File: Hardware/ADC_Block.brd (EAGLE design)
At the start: 30.5 x 44.5 mm, 33 parts, among them U1 ADS1015, U2 PCA9306, U3 3.3V

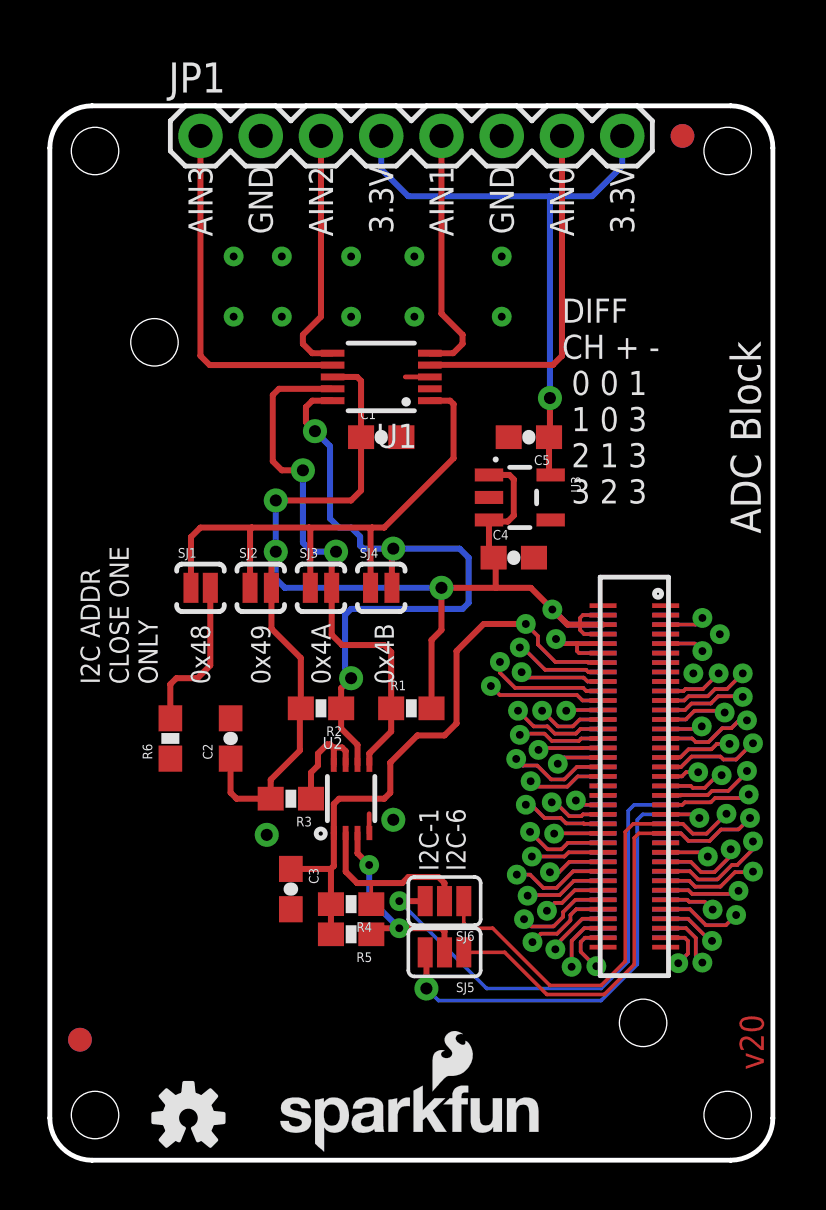
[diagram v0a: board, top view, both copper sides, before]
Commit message: moved differential pair chart and added separation lines
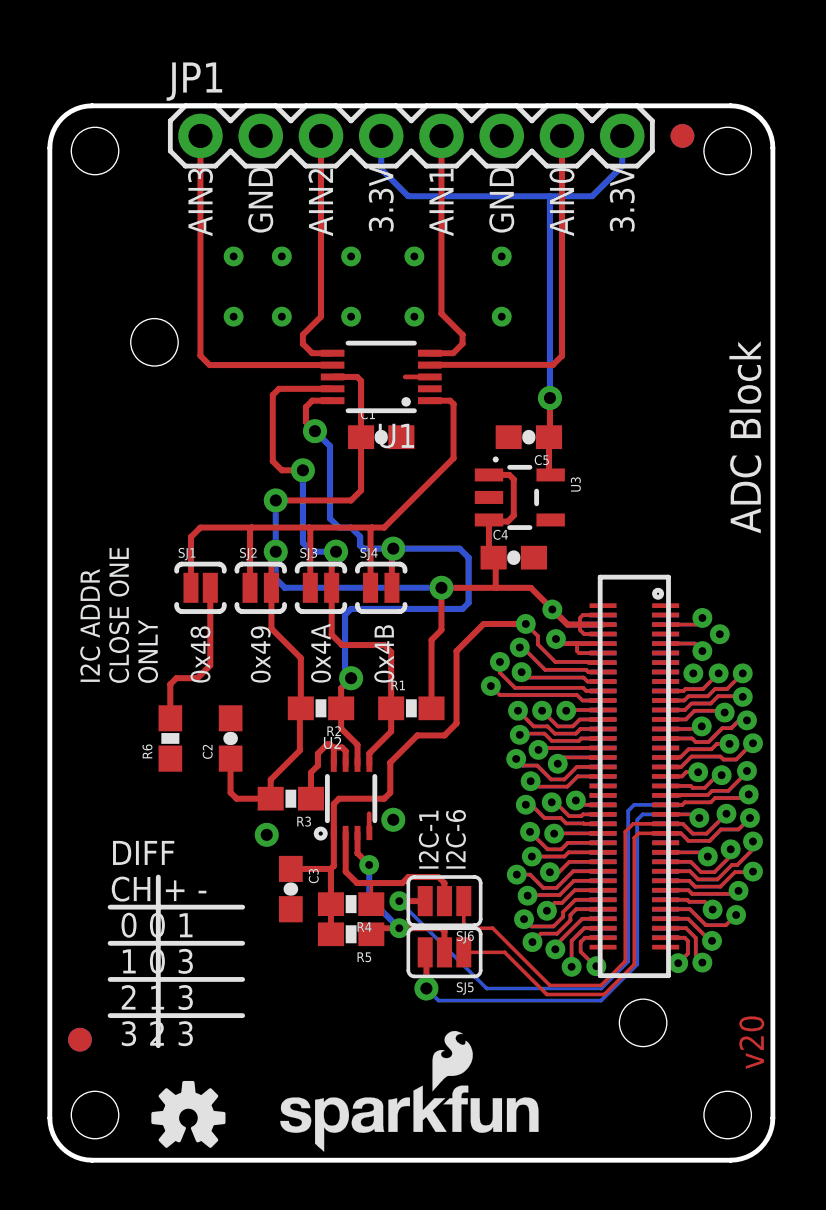
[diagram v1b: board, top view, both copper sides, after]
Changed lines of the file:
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@@
 <?xml version="1.0" encoding="utf-8"?>
 <!DOCTYPE eagle SYSTEM "eagle.dtd">
-<eagle version="7.3.0">
+<eagle version="7.1.0">
 <drawing>
 <settings>
@@
 <setting verticaltext="up"/>
 </settings>
-<grid distance="0.05" unitdist="inch" unit="inch" style="lines" multiple="1" display="yes" altdistance="0.005" altunitdist="inch" altunit="inch"/>
+<grid distance="0.01" unitdist="inch" unit="inch" style="lines" multiple="1" display="yes" altdistance="0.005" altunitdist="inch" altunit="inch"/>
 <layers>
 <layer number="1" name="Top" color="4" fill="1" visible="yes" active="yes"/>
-<layer number="2" name="Route2" color="1" fill="3" visible="no" active="yes"/>
-<layer number="15" name="Route15" color="4" fill="6" visible="no" active="yes"/>
+<layer number="2" name="Route2" color="1" fill="3" visible="yes" active="yes"/>
+<layer number="15" name="Route15" color="4" fill="6" visible="yes" active="yes"/>
 <layer number="16" name="Bottom" color="1" fill="1" visible="yes" active="yes"/>
 <layer number="17" name="Pads" color="2" fill="1" visible="yes" active="yes"/>
@@
 <layer number="23" name="tOrigins" color="15" fill="1" visible="yes" active="yes"/>
 <layer number="24" name="bOrigins" color="15" fill="1" visible="yes" active="yes"/>
-<layer number="25" name="tNames" color="7" fill="1" visible="no" active="yes"/>
-<layer number="26" name="bNames" color="7" fill="1" visible="no" active="yes"/>
-<layer number="27" name="tValues" color="7" fill="1" visible="no" active="yes"/>
-<layer number="28" name="bValues" color="7" fill="1" visible="no" active="yes"/>
-<layer number="29" name="tStop" color="7" fill="3" visible="no" active="yes"/>
-<layer number="30" name="bStop" color="7" fill="6" visible="no" active="yes"/>
-<layer number="31" name="tCream" color="7" fill="4" visible="no" active="yes"/>
-<layer number="32" name="bCream" color="7" fill="5" visible="no" active="yes"/>
-<layer number="39" name="tKeepout" color="4" fill="11" visible="no" active="yes"/>
-<layer number="40" name="bKeepout" color="1" fill="11" visible="no" active="yes"/>
-<layer number="41" name="tRestrict" color="4" fill="10" visible="no" active="yes"/>
-<layer number="42" name="bRestrict" color="1" fill="10" visible="no" active="yes"/>
-<layer number="43" name="vRestrict" color="2" fill="10" visible="no" active="yes"/>
-<layer number="44" name="Drills" color="7" fill="1" visible="no" active="yes"/>
+<layer number="25" name="tNames" color="7" fill="1" visible="yes" active="yes"/>
+<layer number="26" name="bNames" color="7" fill="1" visible="yes" active="yes"/>
+<layer number="27" name="tValues" color="7" fill="1" visible="yes" active="yes"/>
+<layer number="28" name="bValues" color="7" fill="1" visible="yes" active="yes"/>
+<layer number="29" name="tStop" color="7" fill="3" visible="yes" active="yes"/>
+<layer number="30" name="bStop" color="7" fill="6" visible="yes" active="yes"/>
+<layer number="31" name="tCream" color="7" fill="4" visible="yes" active="yes"/>
+<layer number="32" name="bCream" color="7" fill="5" visible="yes" active="yes"/>
+<layer number="39" name="tKeepout" color="4" fill="11" visible="yes" active="yes"/>
+<layer number="40" name="bKeepout" color="1" fill="11" visible="yes" active="yes"/>
+<layer number="41" name="tRestrict" color="4" fill="10" visible="yes" active="yes"/>
+<layer number="42" name="bRestrict" color="1" fill="10" visible="yes" active="yes"/>
+<layer number="43" name="vRestrict" color="2" fill="10" visible="yes" active="yes"/>
+<layer number="44" name="Drills" color="7" fill="1" visible="yes" active="yes"/>
 <layer number="45" name="Holes" color="7" fill="1" visible="yes" active="yes"/>
-<layer number="46" name="Milling" color="3" fill="1" visible="no" active="yes"/>
-<layer number="47" name="Measures" color="7" fill="1" visible="no" active="yes"/>
+<layer number="46" name="Milling" color="3" fill="1" visible="yes" active="yes"/>
+<layer number="47" name="Measures" color="7" fill="1" visible="yes" active="yes"/>
 <layer number="51" name="tDocu" color="6" fill="1" visible="yes" active="yes"/>
 <layer number="3" name="Route3" color="4" fill="3" visible="no" active="no"/>
@@
 <text x="17.526" y="12.192" size="0.8128" layer="21" font="vector" ratio="15" rot="R90">I2C-6</text>
 <wire x1="13.2334" y1="14.0208" x2="13.2334" y2="13.5763" width="0.127" layer="41"/>
-<text x="21.59" y="27.686" size="1.016" layer="21" font="vector" ratio="15">DIFF
+<text x="2.54" y="4.826" size="1.016" layer="21" font="vector" ratio="15">DIFF
 CH + -
  0 0 1
@@
  2 1 3
  3 2 3</text>
-<text x="27.432" y="27.686" size="1.016" layer="22" font="vector" ratio="15" rot="MR0">DIFF
+<text x="8.89" y="4.318" size="1.016" layer="22" font="vector" ratio="15" rot="MR0">DIFF
 CH + -
  0 0 1
@@
  2 1 3
  3 2 3</text>
+<wire x1="4.572" y1="11.938" x2="4.572" y2="4.826" width="0.2032" layer="21"/>
+<wire x1="2.54" y1="10.668" x2="8.128" y2="10.668" width="0.2032" layer="21"/>
+<wire x1="2.54" y1="9.144" x2="8.128" y2="9.144" width="0.2032" layer="21"/>
+<wire x1="2.54" y1="7.62" x2="8.128" y2="7.62" width="0.2032" layer="21"/>
+<wire x1="2.54" y1="6.096" x2="8.128" y2="6.096" width="0.2032" layer="21"/>
+<wire x1="3.302" y1="10.16" x2="8.89" y2="10.16" width="0.2032" layer="22"/>
+<wire x1="6.858" y1="11.43" x2="6.858" y2="4.318" width="0.2032" layer="22"/>
+<wire x1="3.302" y1="8.636" x2="8.89" y2="8.636" width="0.2032" layer="22"/>
+<wire x1="3.302" y1="7.112" x2="8.89" y2="7.112" width="0.2032" layer="22"/>
+<wire x1="3.302" y1="5.588" x2="8.89" y2="5.588" width="0.2032" layer="22"/>
 </plain>
 <attributes>
@@
 <via x="9.144" y="13.716" extent="1-16" drill="0.508"/>
 <wire x1="16.02" y1="33.02" x2="14.986" y2="33.02" width="0.2032" layer="1"/>
+<wire x1="25.96" y1="21.3798" x2="25.96" y2="21.38" width="0" layer="19" extent="1-16"/>
+<wire x1="25.96" y1="20.98" x2="25.96" y2="21.38" width="0" layer="19" extent="16-16"/>
+<wire x1="25.96" y1="20.9798" x2="25.96" y2="20.98" width="0" layer="19" extent="1-16"/>
+<wire x1="25.96" y1="20.58" x2="25.96" y2="20.98" width="0" layer="19" extent="16-16"/>
+<wire x1="25.96" y1="20.5798" x2="25.96" y2="20.58" width="0" layer="19" extent="1-16"/>
+<wire x1="25.96" y1="20.18" x2="25.96" y2="20.58" width="0" layer="19" extent="16-16"/>
+<wire x1="25.96" y1="20.1798" x2="25.96" y2="20.18" width="0" layer="19" extent="1-16"/>
+<wire x1="25.96" y1="22.1798" x2="25.96" y2="21.38" width="0" layer="19" extent="1-16"/>
+<wire x1="27.1272" y1="20.5232" x2="25.96" y2="20.58" width="0" layer="19" extent="16-16"/>
 </signal>
 <signal name="VSYS">

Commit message: replaces output capacitor on the 3.3v regulator with 2.2uF
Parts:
- C5: value 0.1uF -> 2.2uF
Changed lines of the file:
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@@
 <attribute name="PROD_ID" value="CAP-00810" x="19.558" y="25.4" size="1.778" layer="27" display="off"/>
 </element>
-<element name="C5" library="SparkFun-Capacitors" package="0603-CAP" value="0.1uF" x="20.193" y="30.48" rot="R180">
-<attribute name="PROD_ID" value="CAP-00810" x="20.193" y="30.48" size="1.778" layer="27" rot="R180" display="off"/>
+<element name="C5" library="SparkFun-Capacitors" package="0603-CAP" value="2.2uF" x="20.193" y="30.48" rot="R180">
+<attribute name="PROD_ID" value="CAP-07888" x="20.193" y="30.48" size="1.778" layer="27" rot="R180" display="off"/>
 </element>
 <element name="SJ5" library="SparkFun-Passives" package="PAD-JUMPER-3-2OF3_NC_BY_PASTE_YES_SILK_FULL_BOX" value="SDA_SEL" x="16.637" y="8.763" rot="R180"/>

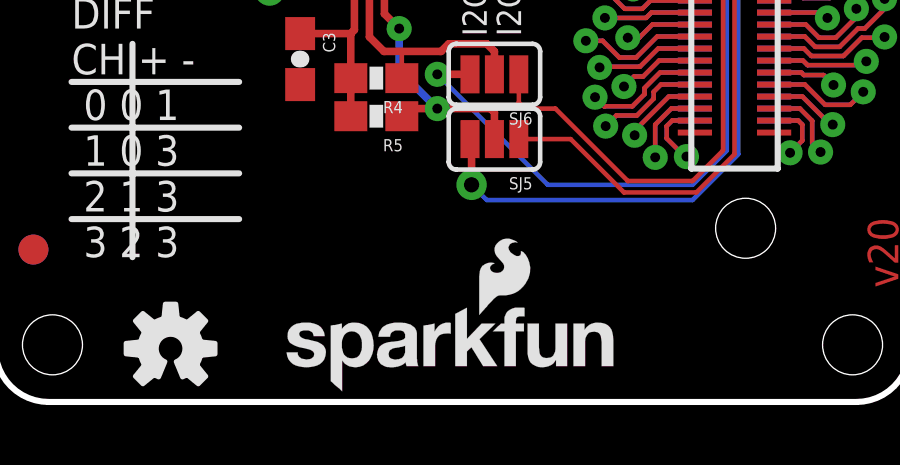
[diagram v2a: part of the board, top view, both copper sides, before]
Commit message: fixed thermal issue preventing gnd pour to connect with pads
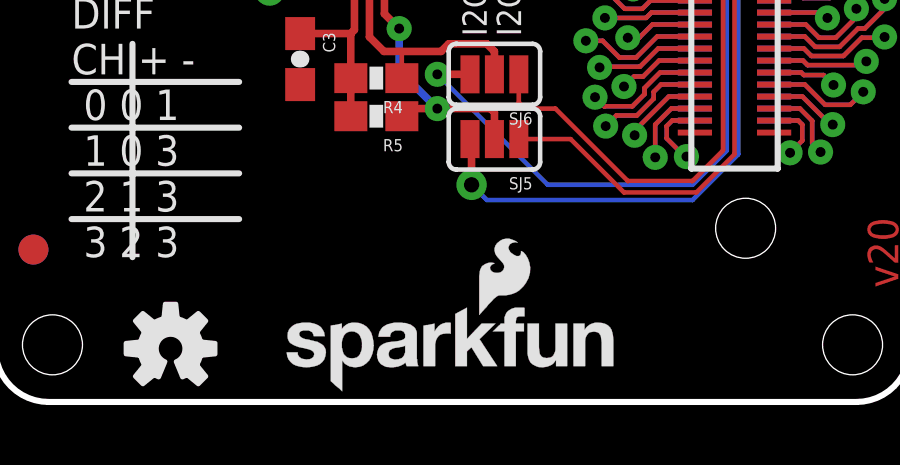
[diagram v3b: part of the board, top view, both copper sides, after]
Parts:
- FRAME1, FRAME2: value (none) -> FRAME-LETTER
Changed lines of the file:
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@@
 <layer number="112" name="tSilk" color="7" fill="1" visible="no" active="no"/>
 <layer number="113" name="IDFDebug" color="4" fill="1" visible="no" active="no"/>
+<layer number="114" name="Badge_Outline" color="11" fill="1" visible="no" active="no"/>
 <layer number="116" name="Patch_BOT" color="9" fill="4" visible="no" active="no"/>
+<layer number="118" name="Rect_Pads" color="7" fill="1" visible="yes" active="yes"/>
 <layer number="121" name="_tsilk" color="7" fill="1" visible="no" active="no"/>
 <layer number="122" name="_bsilk" color="7" fill="1" visible="no" active="no"/>
@@
 <param name="rvMicroViaOuter" value="0.25"/>
 <param name="rvMicroViaInner" value="0.25"/>
-<param name="rlMinPadTop" value="12mil"/>
+<param name="rlMinPadTop" value="6mil"/>
 <param name="rlMaxPadTop" value="20mil"/>
 <param name="rlMinPadInner" value="10mil"/>
@@
 <param name="srMinRoundness" value="0mil"/>
 <param name="srMaxRoundness" value="0mil"/>
-<param name="slThermalIsolate" value="10mil"/>
+<param name="slThermalIsolate" value="8mil"/>
 <param name="slThermalsForVias" value="0"/>
 <param name="dpMaxLengthDifference" value="10mm"/>
@@
 </autorouter>
 <elements>
-<element name="FRAME1" library="SparkFun-Aesthetics" package="CREATIVE_COMMONS" value="" x="-1.27" y="-13.97">
-<attribute name="VERSION" value="v01" x="-1.27" y="-13.97" size="1.778" layer="27" display="off"/>
-<attribute name="DESIGNER" value="NAME" x="-1.27" y="-13.97" size="1.778" layer="27" display="off"/>
-</element>
+<element name="FRAME1" library="SparkFun-Aesthetics" package="CREATIVE_COMMONS" value="FRAME-LETTER" x="-1.27" y="-13.97"/>
 <element name="LOGO2" library="SparkFun-Aesthetics" package="OSHW-LOGO-S" value="OSHW-LOGOS" x="5.842" y="1.778" rot="MR0"/>
 <element name="LOGO3" library="SparkFun-Aesthetics" package="SFE_LOGO_NAME_FLAME_.1" value="SFE_LOGO_NAME_FLAME.1_INCH" x="21.082" y="0.254" rot="MR0"/>
 <element name="JP2" library="SparkFun-Boards" package="EDISON_DAUGHTER" value="EDISON_CONNECTOR_FULLMOUNTING_HOLES" x="27.94" y="3.81" rot="MR0"/>
 <element name="JP3" library="SparkFun-Boards" package="DF40C-70DP-0.4(51)" value="EDISON_CONNECTOR_FULLHEADER" x="24.64" y="16.1798" rot="MR90"/>
-<element name="FRAME2" library="SparkFun-Aesthetics" package="CREATIVE_COMMONS" value="" x="-1.27" y="-13.97">
-<attribute name="VERSION" value="v01" x="-1.27" y="-13.97" size="1.778" layer="27" display="off"/>
-<attribute name="DESIGNER" value="NAME" x="-1.27" y="-13.97" size="1.778" layer="27" display="off"/>
-</element>
+<element name="FRAME2" library="SparkFun-Aesthetics" package="CREATIVE_COMMONS" value="FRAME-LETTER" x="-1.27" y="-13.97"/>
 <element name="C1" library="SparkFun-Capacitors" package="0603-CAP" value="0.1uF" x="13.97" y="30.48">
 <attribute name="PROD_ID" value="CAP-00810" x="13.97" y="53.34" size="1.778" layer="27" font="vector" ratio="15" display="off"/>
@@
 <via x="9.144" y="13.716" extent="1-16" drill="0.508"/>
 <wire x1="16.02" y1="33.02" x2="14.986" y2="33.02" width="0.2032" layer="1"/>
-<wire x1="25.96" y1="21.3798" x2="25.96" y2="21.38" width="0" layer="19" extent="1-16"/>
-<wire x1="25.96" y1="20.98" x2="25.96" y2="21.38" width="0" layer="19" extent="16-16"/>
-<wire x1="25.96" y1="20.9798" x2="25.96" y2="20.98" width="0" layer="19" extent="1-16"/>
-<wire x1="25.96" y1="20.58" x2="25.96" y2="20.98" width="0" layer="19" extent="16-16"/>
-<wire x1="25.96" y1="20.5798" x2="25.96" y2="20.58" width="0" layer="19" extent="1-16"/>
-<wire x1="25.96" y1="20.18" x2="25.96" y2="20.58" width="0" layer="19" extent="16-16"/>
-<wire x1="25.96" y1="20.1798" x2="25.96" y2="20.18" width="0" layer="19" extent="1-16"/>
-<wire x1="25.96" y1="22.1798" x2="25.96" y2="21.38" width="0" layer="19" extent="1-16"/>
-<wire x1="27.1272" y1="20.5232" x2="25.96" y2="20.58" width="0" layer="19" extent="16-16"/>
 </signal>
 <signal name="VSYS">

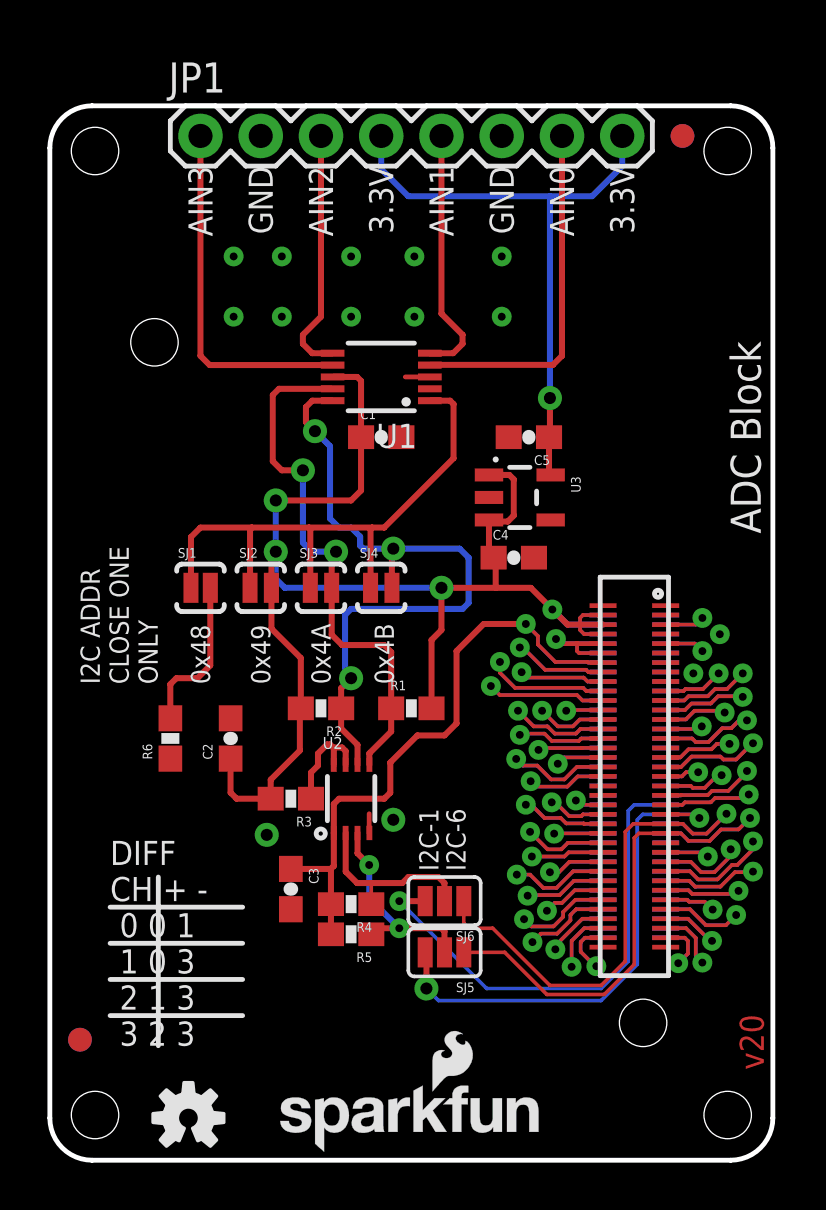
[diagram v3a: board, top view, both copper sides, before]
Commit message: Added resistor to output cap on LDO. Changed header to locking male header.
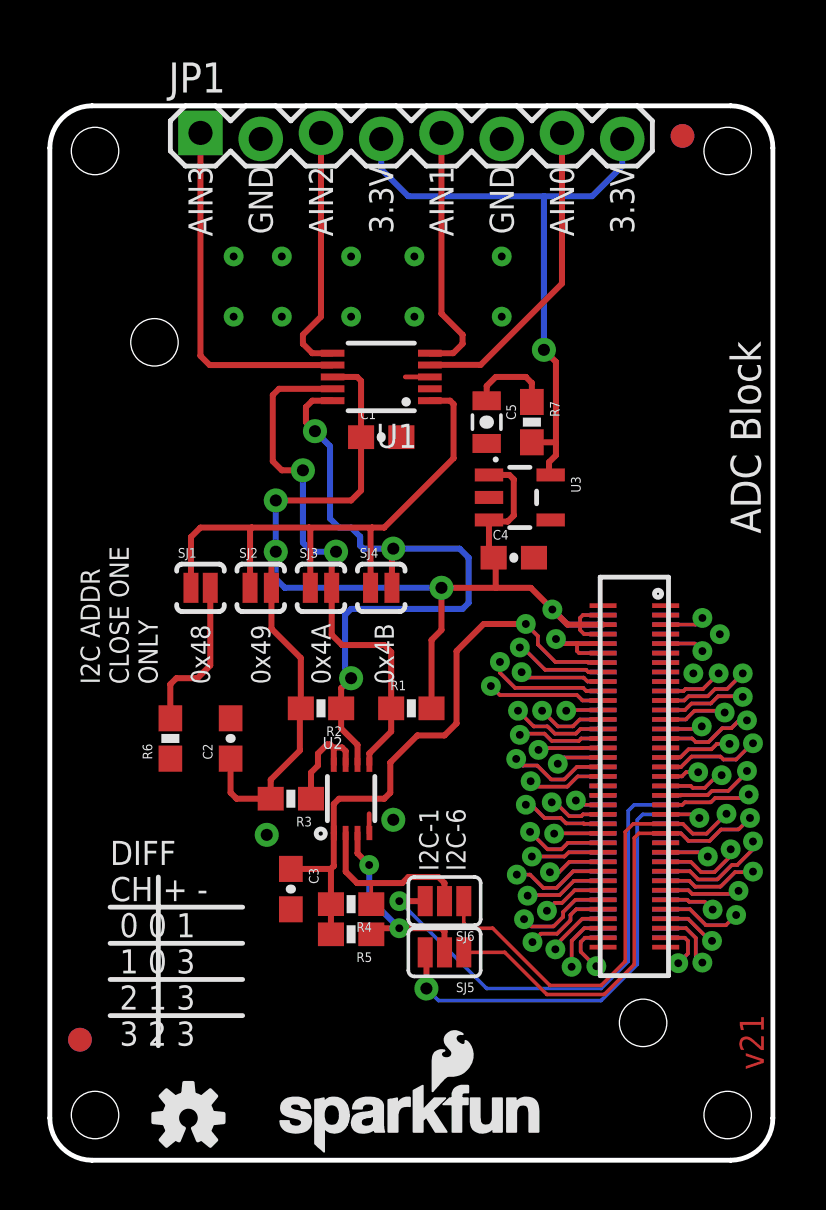
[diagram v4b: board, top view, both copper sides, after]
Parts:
- added R7: 0.27, SparkFun-Resistors:0603-RES
- C5: value 2.2uF -> 10uF; device SparkFun-Capacitors:0603-CAP -> SparkFun-Capacitors:0805-CAP
- JP1: device SparkFun-Connectors:1X08_ROUND -> SparkFun-Connectors:1X08_LOCK
- R4, R5: value DNP -> 2.2k
- moved C5 1.89 mm to (18.4, 31.1), turned to 270 degrees
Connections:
- new net N$5: C5.1, R7.1
- net VREF: now also R7.2; no longer C5.1
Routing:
- net N$5: track 0.00 -> 3.59 mm
- net A0+/AIN0: track 15.0 -> 13.3 mm
- net VREF: track 25.6 -> 26.7 mm
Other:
- board text added: "Revised 10/15 - Shawn Hymel"
- board text added: "v21"
- board text added: "x6"
- board text removed: "v20"
